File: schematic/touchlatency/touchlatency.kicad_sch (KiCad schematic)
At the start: 18 parts, among them J1 Photodiode, J2 Electrode, J3 Screw_Terminal_01x02, J4 Seriel, J5 Conn_01x06_Socket, J6 Conn_01x02_Socket, J7 Conn_01x02_Socket, Q1 2N2222, U1 WeMos_D1_mini, U3 LM78M05_TO220

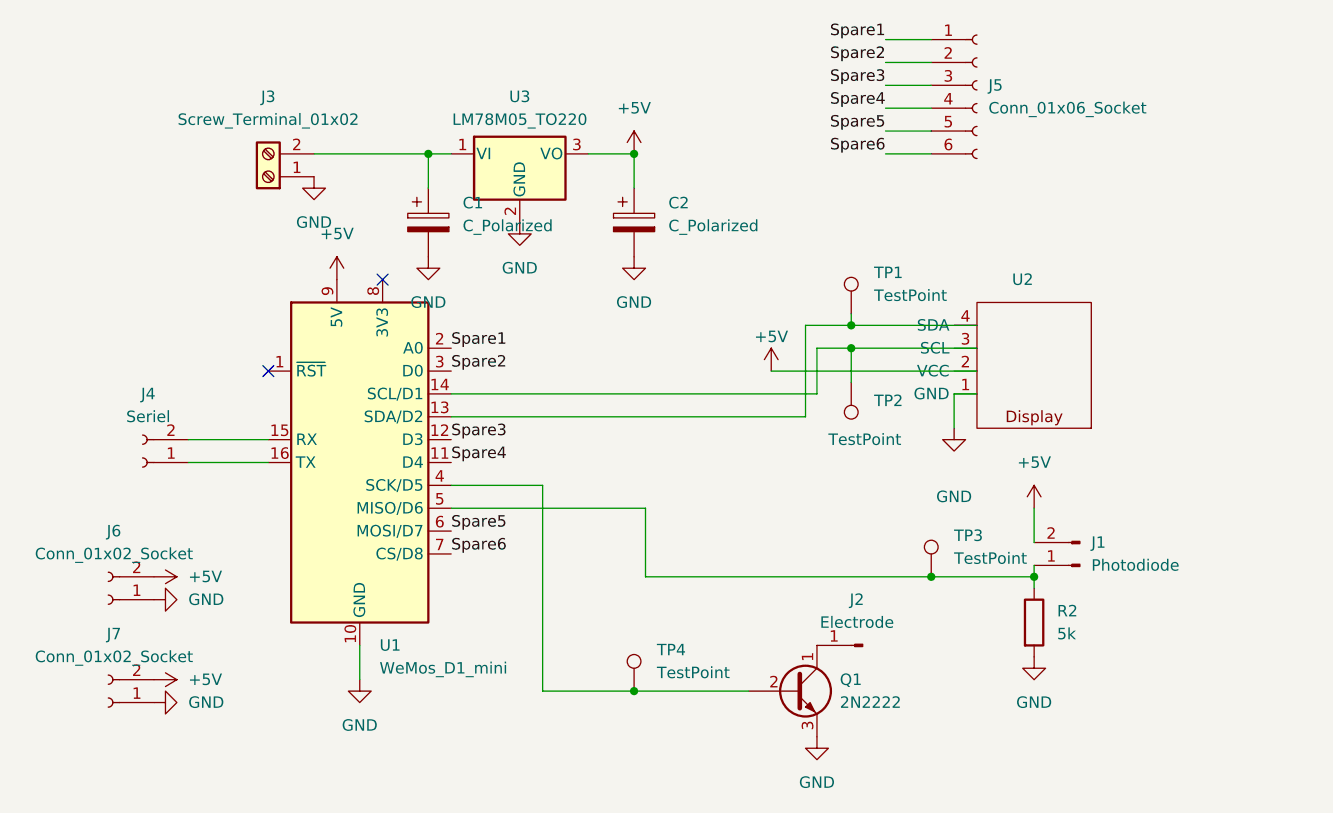
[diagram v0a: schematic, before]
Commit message: Rev B Phototransistor Update
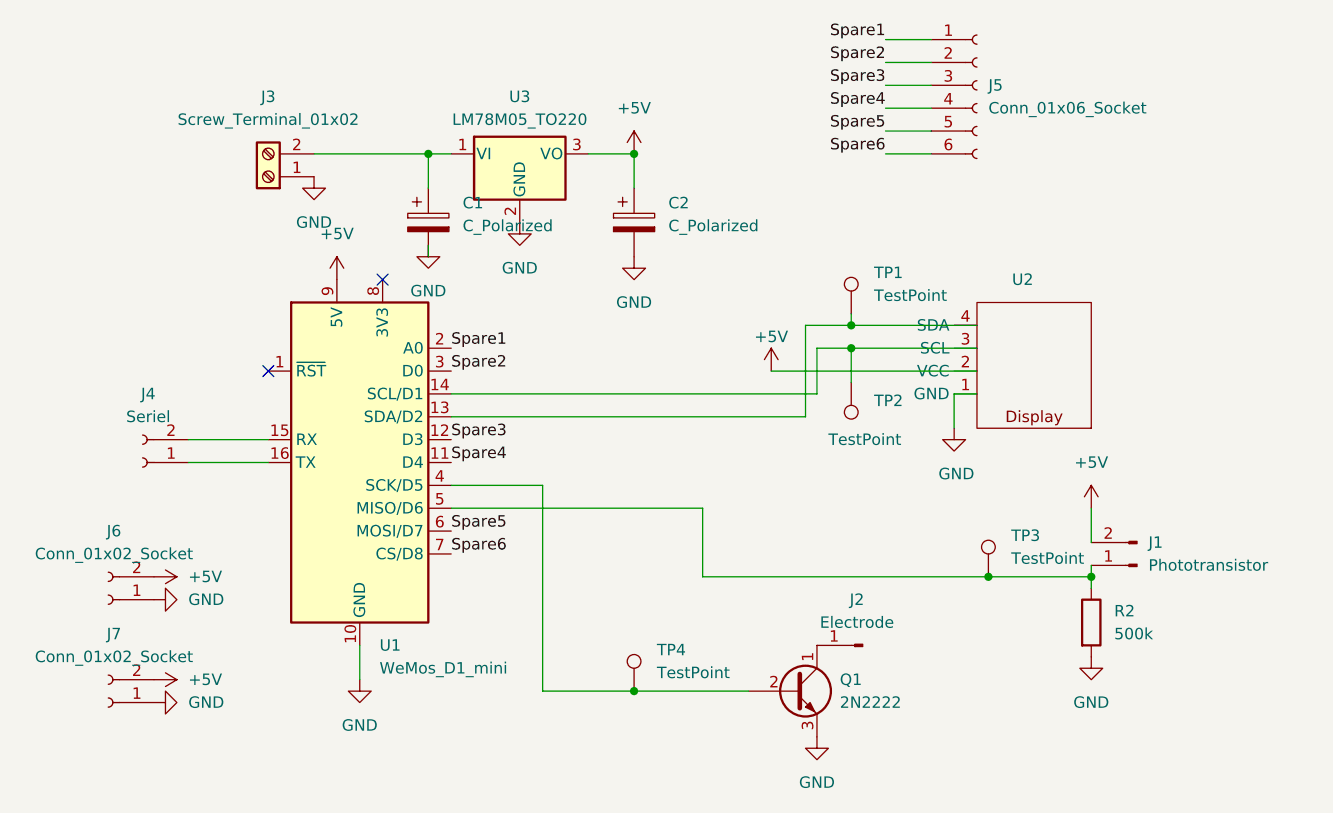
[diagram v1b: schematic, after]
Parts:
- J1: value Photodiode -> Phototransistor
- R2: value 5k -> 500k
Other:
- moved on the sheet: J1, R2, TP3
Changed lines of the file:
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@@
 	(title_block
 		(title "Touch-O-Mat 3000")
-		(rev "A")
+		(rev "B")
 		(company "Flo GmbH")
 	)
 	(junction
-		(at 195.58 120.65)
+		(at 201.93 120.65)
 		(diameter 0)
 		(color 0 0 0 0)
 	)
 	(junction
-		(at 184.15 120.65)
+		(at 190.5 120.65)
 		(diameter 0)
 		(color 0 0 0 0)
@@
 	(wire
 		(pts
-			(xy 152.4 120.65) (xy 184.15 120.65)
+			(xy 158.75 120.65) (xy 190.5 120.65)
+		)
+		(stroke
+			(width 0)
+			(type default)
+		)
+	)
+	(wire
+		(pts
+			(xy 128.27 83.82) (xy 128.27 85.09)
 		)
 		(stroke
@@
 	(wire
 		(pts
-			(xy 152.4 113.03) (xy 130.81 113.03)
+			(xy 158.75 113.03) (xy 130.81 113.03)
 		)
 		(stroke
@@
 	(wire
 		(pts
-			(xy 195.58 113.03) (xy 195.58 116.84)
+			(xy 201.93 113.03) (xy 201.93 116.84)
 		)
 		(stroke
@@
 	(wire
 		(pts
-			(xy 195.58 119.38) (xy 195.58 120.65)
+			(xy 201.93 119.38) (xy 201.93 120.65)
 		)
 		(stroke
@@
 	(wire
 		(pts
-			(xy 152.4 120.65) (xy 152.4 113.03)
+			(xy 158.75 120.65) (xy 158.75 113.03)
 		)
 		(stroke
@@
 	(wire
 		(pts
-			(xy 195.58 120.65) (xy 195.58 121.92)
+			(xy 201.93 120.65) (xy 201.93 121.92)
 		)
 		(stroke
@@
 	(wire
 		(pts
-			(xy 184.15 120.65) (xy 195.58 120.65)
+			(xy 190.5 120.65) (xy 201.93 120.65)
 		)
 		(stroke
@@
 	(symbol
 		(lib_id "power:GND")
-		(at 128.27 85.09 0)
+		(at 128.27 83.82 0)
 		(unit 1)
 		(exclude_from_sim no)
@@
 		(fields_autoplaced yes)
 		(property "Reference" "#PWR015"
-			(at 128.27 91.44 0)
+			(at 128.27 90.17 0)
 			(effects
 				(font
@@
 		)
 		(property "Value" "GND"
-			(at 128.27 90.17 0)
+			(at 128.27 88.9 0)
 			(effects
 				(font
@@
 		)
 		(property "Footprint" ""
-			(at 128.27 85.09 0)
+			(at 128.27 83.82 0)
 			(effects
 				(font
@@
 		)
 		(property "Datasheet" ""
-			(at 128.27 85.09 0)
-			(effects
-				(font
-					(size 1.27 1.27)
-				)
-				(hide yes)
-			)
-		)
-		(property "Description" ""
-			(at 128.27 85.09 0)
+			(at 128.27 83.82 0)
+			(effects
+				(font
+					(size 1.27 1.27)
+				)
+				(hide yes)
+			)
+		)
+		(property "Description" ""
+			(at 128.27 83.82 0)
 			(effects
 				(font
@@
 	(symbol
 		(lib_id "Connector:Conn_01x02_Pin")
-		(at 200.66 119.38 180)
+		(at 207.01 119.38 180)
 		(unit 1)
 		(exclude_from_sim no)
@@
 		(fields_autoplaced yes)
 		(property "Reference" "J1"
-			(at 201.93 116.84 0)
+			(at 208.28 116.8399 0)
 			(effects
 				(font
@@
 			)
 		)
-		(property "Value" "Photodiode"
-			(at 201.93 119.38 0)
+		(property "Value" "Phototransistor"
+			(at 208.28 119.3799 0)
 			(effects
 				(font
@@
 		)
 		(property "Footprint" "Connector_PinHeader_2.54mm:PinHeader_1x02_P2.54mm_Vertical"
-			(at 200.66 119.38 0)
+			(at 207.01 119.38 0)
 			(effects
 				(font
@@
 		)
 		(property "Datasheet" "~"
-			(at 200.66 119.38 0)
-			(effects
-				(font
-					(size 1.27 1.27)
-				)
-				(hide yes)
-			)
-		)
-		(property "Description" ""
-			(at 200.66 119.38 0)
+			(at 207.01 119.38 0)
+			(effects
+				(font
+					(size 1.27 1.27)
+				)
+				(hide yes)
+			)
+		)
+		(property "Description" ""
+			(at 207.01 119.38 0)
 			(effects
 				(font
@@
 		)
 		(property "Value" "GND"
-			(at 186.69 111.76 0)
+			(at 186.944 109.22 0)
 			(effects
 				(font
@@
 	(symbol
 		(lib_id "power:+5V")
-		(at 195.58 113.03 0)
+		(at 201.93 113.03 0)
 		(unit 1)
 		(exclude_from_sim no)
@@
 		(fields_autoplaced yes)
 		(property "Reference" "#PWR04"
-			(at 195.58 116.84 0)
+			(at 201.93 116.84 0)
 			(effects
 				(font
@@
 		)
 		(property "Value" "+5V"
-			(at 195.58 107.95 0)
+			(at 201.93 107.95 0)
 			(effects
 				(font
@@
 		)
 		(property "Footprint" ""
-			(at 195.58 113.03 0)
+			(at 201.93 113.03 0)
 			(effects
 				(font
@@
 		)
 		(property "Datasheet" ""
-			(at 195.58 113.03 0)
-			(effects
-				(font
-					(size 1.27 1.27)
-				)
-				(hide yes)
-			)
-		)
-		(property "Description" ""
-			(at 195.58 113.03 0)
+			(at 201.93 113.03 0)
+			(effects
+				(font
+					(size 1.27 1.27)
+				)
+				(hide yes)
+			)
+		)
+		(property "Description" ""
+			(at 201.93 113.03 0)
 			(effects
 				(font
@@
 	(symbol
 		(lib_id "Device:R")
-		(at 195.58 125.73 0)
+		(at 201.93 125.73 0)
 		(unit 1)
 		(exclude_from_sim no)
@@
 		(fields_autoplaced yes)
 		(property "Reference" "R2"
-			(at 198.12 124.46 0)
+			(at 204.47 124.46 0)
 			(effects
 				(font
@@
 			)
 		)
-		(property "Value" "5k"
-			(at 198.12 127 0)
+		(property "Value" "500k"
+			(at 204.47 127 0)
 			(effects
 				(font
@@
 		)
 		(property "Footprint" "Resistor_THT:R_Axial_DIN0207_L6.3mm_D2.5mm_P10.16mm_Horizontal"
-			(at 193.802 125.73 90)
+			(at 200.152 125.73 90)
 			(effects
 				(font
@@
 		)
 		(property "Datasheet" "~"
-			(at 195.58 125.73 0)
-			(effects
-				(font
-					(size 1.27 1.27)
-				)
-				(hide yes)
-			)
-		)
-		(property "Description" ""
-			(at 195.58 125.73 0)
+			(at 201.93 125.73 0)
+			(effects
+				(font
+					(size 1.27 1.27)
+				)
+				(hide yes)
+			)
+		)
+		(property "Description" ""
+			(at 201.93 125.73 0)
 			(effects
 				(font
@@
 	(symbol
 		(lib_id "Connector:TestPoint")
-		(at 184.15 120.65 0)
+		(at 190.5 120.65 0)
 		(unit 1)
 		(exclude_from_sim no)
@@
 		(fields_autoplaced yes)
 		(property "Reference" "TP3"
-			(at 186.69 116.078 0)
+			(at 193.04 116.078 0)
 			(effects
 				(font
@@
 		)
 		(property "Value" "TestPoint"
-			(at 186.69 118.618 0)
+			(at 193.04 118.618 0)
 			(effects
 				(font
@@
 		)
 		(property "Footprint" "TestPoint:TestPoint_Pad_D2.0mm"
-			(at 189.23 120.65 0)
+			(at 195.58 120.65 0)
 			(effects
 				(font
@@
 		)
 		(property "Datasheet" "~"
-			(at 189.23 120.65 0)
-			(effects
-				(font
-					(size 1.27 1.27)
-				)
-				(hide yes)
-			)
-		)
-		(property "Description" ""
-			(at 184.15 120.65 0)
+			(at 195.58 120.65 0)
+			(effects
+				(font
+					(size 1.27 1.27)
+				)
+				(hide yes)
+			)
+		)
+		(property "Description" ""
+			(at 190.5 120.65 0)
 			(effects
 				(font
@@
 	(symbol
 		(lib_id "power:GND")
-		(at 195.58 129.54 0)
+		(at 201.93 129.54 0)
 		(unit 1)
 		(exclude_from_sim no)
@@
 		(fields_autoplaced yes)
 		(property "Reference" "#PWR05"
-			(at 195.58 135.89 0)
+			(at 201.93 135.89 0)
 			(effects
 				(font
@@
 		)
 		(property "Value" "GND"
-			(at 195.58 134.62 0)
+			(at 201.93 134.62 0)
 			(effects
 				(font
@@
 		)
 		(property "Footprint" ""
-			(at 195.58 129.54 0)
+			(at 201.93 129.54 0)
 			(effects
 				(font
@@
 		)
 		(property "Datasheet" ""
-			(at 195.58 129.54 0)
-			(effects
-				(font
-					(size 1.27 1.27)
-				)
-				(hide yes)
-			)
-		)
-		(property "Description" ""
-			(at 195.58 129.54 0)
-			(effects
-				(font
+			(at 201.93 129.54 0)
+			(effects
+				(font
+					(size 1.27 1.27)
+				)
+				(hide yes)
+			)
+		)
+		(property "Description" ""
+			(at 201.93 129.54 0)
+			(effects
+				(font
